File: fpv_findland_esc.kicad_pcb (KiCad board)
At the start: 6 copper layers, 36 x 47.4 mm, 166 parts, among them J1 Conn_01x01_Pin, J10 Conn_01x01_Pin, J11 Conn_01x01_Pin, J12 Conn_01x01_Pin, J13 Conn_01x01_Pin, J2 Conn_01x06, J3 Conn_01x01_Pin, J4 Conn_01x01_Pin, J5 Conn_01x01_Pin, J6 Conn_01x01_Pin, J7 Conn_01x01_Pin, J8 Conn_01x01_Pin, J9 Conn_01x01_Pin, Q1 FDMC8010DC, Q10 FDMC8010DC, Q11 FDMC8010DC, Q12 FDMC8010DC, Q13 FDMC8010DC, Q14 FDMC8010DC, Q15 FDMC8010DC, Q16 FDMC8010DC, Q17 FDMC8010DC, Q18 FDMC8010DC, Q19 FDMC8010DC, Q2 FDMC8010DC, Q20 FDMC8010DC, Q21 FDMC8010DC, Q22 FDMC8010DC, Q23 FDMC8010DC, Q24 FDMC8010DC, Q3 FDMC8010DC, Q4 FDMC8010DC, Q5 FDMC8010DC, Q6 FDMC8010DC, Q7 FDMC8010DC, Q8 FDMC8010DC, Q9 FDMC8010DC, U1 GD32E230G8U6, U10 DRV8300D, U2 WL2851E33, U3 GD32E230G8U6, U4 GD32E230G8U6, U5 AP63200, U6 GD32E230G8U6, U7 DRV8300D, U8 DRV8300D, U9 DRV8300D

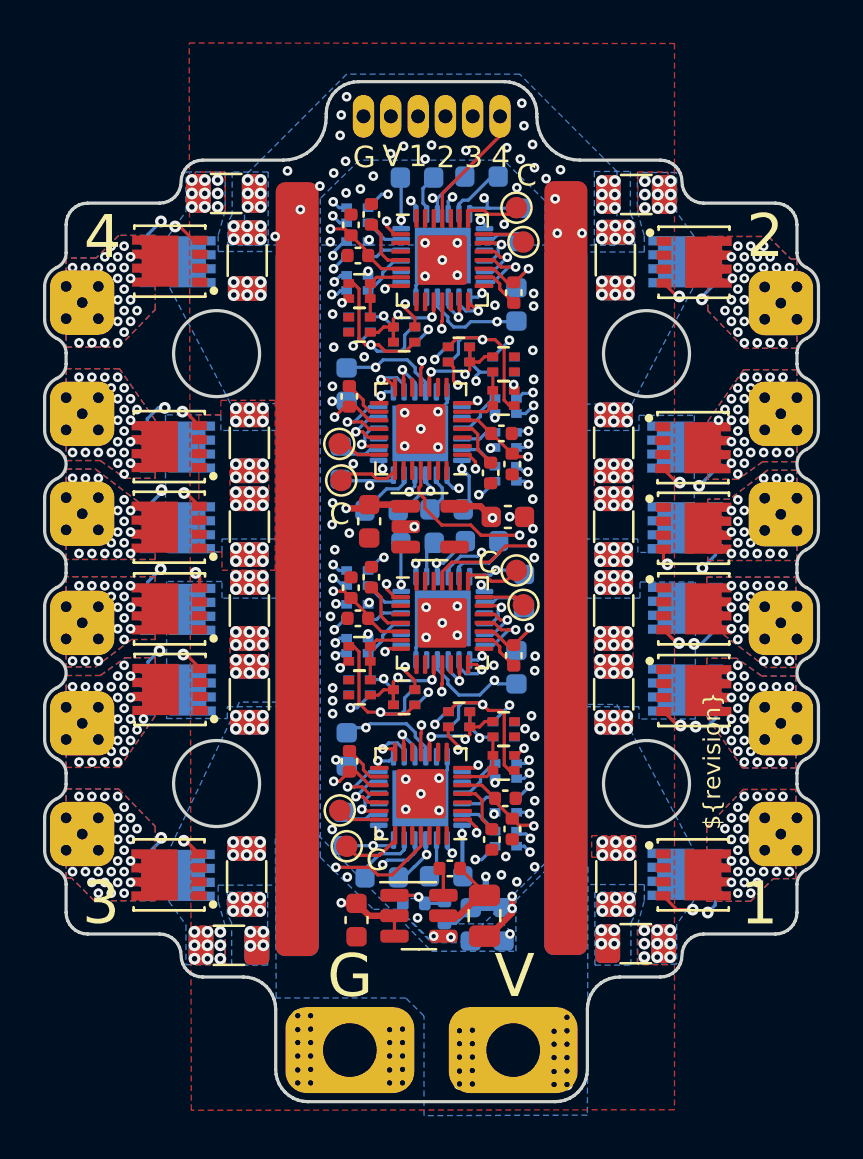
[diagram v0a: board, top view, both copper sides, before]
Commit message: Removed some sharp corners etc
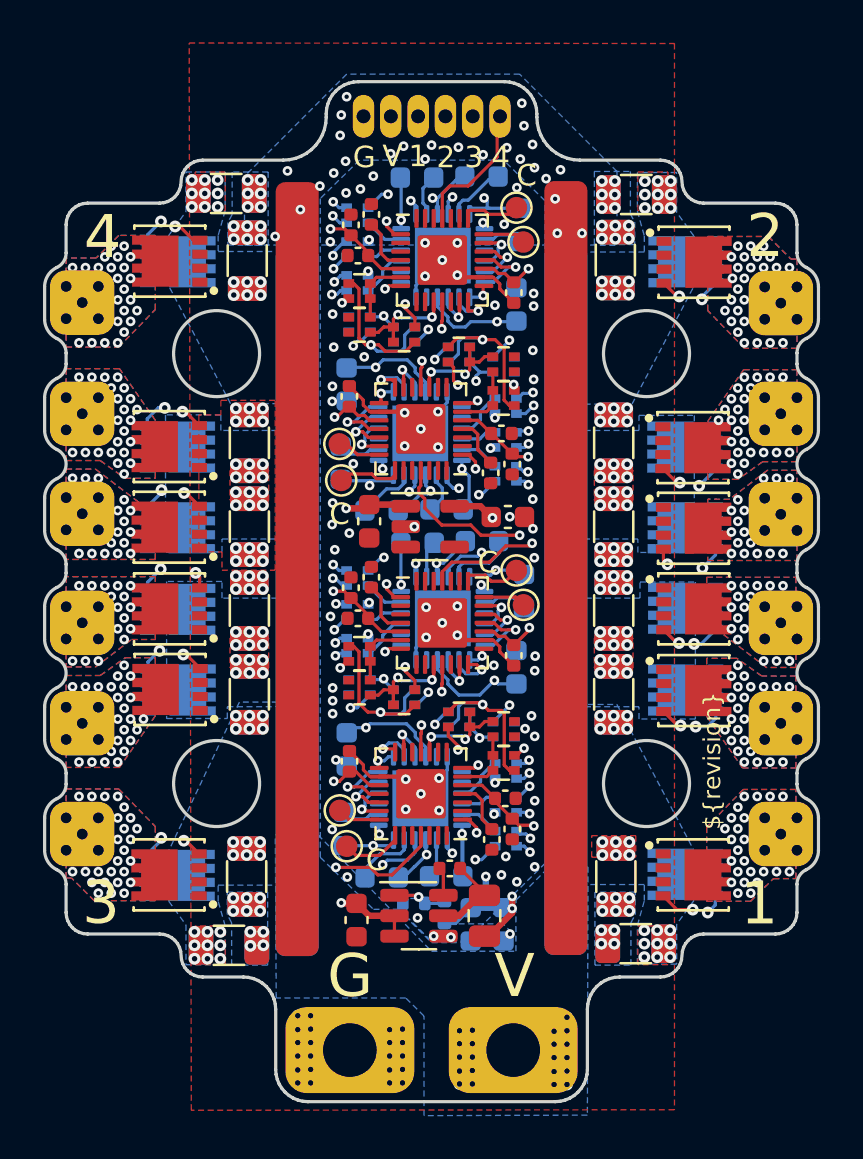
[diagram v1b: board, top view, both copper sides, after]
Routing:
- net GND: track 12.7 -> 17.8 mm, vias 207 -> 208
